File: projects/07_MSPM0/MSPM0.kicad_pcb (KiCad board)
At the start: 2 copper layers, 0 parts

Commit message: MSPM0 - Complete schematic, pass ERC checks, import footprints to PCB.
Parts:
- added C1: 10u, Capacitor_SMD:C_1206_3216Metric_Pad1.33x1.80mm_HandSolder, F.Cu at (142.1, 95.8)
- added C10: 10u, Capacitor_SMD:C_1206_3216Metric_Pad1.33x1.80mm_HandSolder, F.Cu at (160.4, 65.0)
- added C11: 470p, Capacitor_SMD:C_0603_1608Metric_Pad1.08x0.95mm_HandSolder, F.Cu at (160.4, 68.3)
- added C12: 470p, Capacitor_SMD:C_0603_1608Metric_Pad1.08x0.95mm_HandSolder, F.Cu at (141.4, 65.4)
- added C13: 470p, Capacitor_SMD:C_0603_1608Metric_Pad1.08x0.95mm_HandSolder, F.Cu at (141.4, 60.2)
- added C14: 100n, Capacitor_SMD:C_0603_1608Metric_Pad1.08x0.95mm_HandSolder, F.Cu at (201.0, 80.2)
- added C15: 100n, Capacitor_SMD:C_0603_1608Metric_Pad1.08x0.95mm_HandSolder, F.Cu at (201.0, 83.6)
- added C16: 1u, Capacitor_SMD:C_1206_3216Metric_Pad1.33x1.80mm_HandSolder, F.Cu at (179.0, 105.0)
- added C18: 10u, Capacitor_SMD:C_1206_3216Metric_Pad1.33x1.80mm_HandSolder, F.Cu at (188.5, 104.9)
- added C2: 15p, Capacitor_SMD:C_0603_1608Metric_Pad1.08x0.95mm_HandSolder, F.Cu at (134.9, 104.0)
- added C3: 470n, Capacitor_SMD:C_0603_1608Metric_Pad1.08x0.95mm_HandSolder, F.Cu at (147.7, 89.0)
- added C4: 470n, Capacitor_SMD:C_0603_1608Metric_Pad1.08x0.95mm_HandSolder, F.Cu at (137.5, 89.2)
- added C5: 470n, Capacitor_SMD:C_0603_1608Metric_Pad1.08x0.95mm_HandSolder, F.Cu at (152.5, 88.2)
- added C6: 15p, Capacitor_SMD:C_0603_1608Metric_Pad1.08x0.95mm_HandSolder, F.Cu at (142.1, 110.0)
- added C7: 470p, Capacitor_SMD:C_0603_1608Metric_Pad1.08x0.95mm_HandSolder, F.Cu at (160.4, 54.9)
- added C8: 470p, Capacitor_SMD:C_0603_1608Metric_Pad1.08x0.95mm_HandSolder, F.Cu at (160.4, 58.3)
- added C9: 10u, Capacitor_SMD:C_1206_3216Metric_Pad1.33x1.80mm_HandSolder, F.Cu at (160.4, 61.6)
- added D1: USBLC6-2SC6, Package_TO_SOT_SMD:SOT-23-6_Handsoldering, F.Cu at (122.5, 64.1)
- added D2: LED, LED_SMD:LED_1206_3216Metric_Pad1.42x1.75mm_HandSolder, F.Cu at (136.8, 70.4)
- added FID1: Fiducial, Fiducial:Fiducial_1mm_Mask2mm, F.Cu at (89.3, 92.5)
- added FID2: Fiducial, Fiducial:Fiducial_1mm_Mask2mm, F.Cu at (89.3, 96.0)
- added FID3: Fiducial, Fiducial:Fiducial_1mm_Mask2mm, F.Cu at (89.3, 99.6)
- added J1: USB_C_Receptacle_USB2.0_16P, Connector_USB:USB_C_Receptacle_G-Switch_GT-USB-7010ASV, F.Cu at (108.3, 66.6)
- added J2: Conn_ARM_SWD_TagConnect_TC2030, Connector:Tag-Connect_TC2030-IDC-FP_2x03_P1.27mm_Vertical, F.Cu at (165.8, 117.8)
- added JP1: SolderJumper_2_Bridged, Jumper:SolderJumper-2_P1.3mm_Bridged_RoundedPad1.0x1.5mm, F.Cu at (194.1, 75.2)
- added JP2: SolderJumper_2_Bridged, Jumper:SolderJumper-2_P1.3mm_Bridged_RoundedPad1.0x1.5mm, F.Cu at (191.4, 75.2)
- added JP3: SolderJumper_2_Bridged, Jumper:SolderJumper-2_P1.3mm_Bridged_RoundedPad1.0x1.5mm, F.Cu at (180.1, 99.8)
- added JP4: SolderJumper_2_Bridged, Jumper:SolderJumper-2_P1.3mm_Bridged_RoundedPad1.0x1.5mm, F.Cu at (182.7, 99.8)
- added JP5: SolderJumper_2_Bridged, Jumper:SolderJumper-2_P1.3mm_Bridged_RoundedPad1.0x1.5mm, F.Cu at (185.3, 99.8)
- added JP6: SolderJumper_2_Bridged, Jumper:SolderJumper-2_P1.3mm_Bridged_RoundedPad1.0x1.5mm, F.Cu at (184.4, 81.2)
- added JP7: SolderJumper_2_Bridged, Jumper:SolderJumper-2_P1.3mm_Bridged_RoundedPad1.0x1.5mm, F.Cu at (184.4, 83.8)
- added MH1: M3, MountingHole:MountingHole_3.2mm_M3_Pad_Via, F.Cu at (83.6, 94.7)
- added MH2: M3, MountingHole:MountingHole_3.2mm_M3_Pad_Via, F.Cu at (83.6, 102.6)
- added MH3: M3, MountingHole:MountingHole_3.2mm_M3_Pad_Via, F.Cu at (83.6, 110.6)
- added MH4: M3, MountingHole:MountingHole_3.2mm_M3_Pad_Via, F.Cu at (83.6, 118.5)
- added R1: 100k 0.1%, Resistor_SMD:R_0603_1608Metric_Pad0.98x0.95mm_HandSolder, F.Cu at (143.9, 99.0)
- added R2: 5k1, Resistor_SMD:R_0603_1608Metric_Pad0.98x0.95mm_HandSolder, F.Cu at (137.7, 93.4)
- added R3: 0R, Resistor_SMD:R_0603_1608Metric_Pad0.98x0.95mm_HandSolder, F.Cu at (152.3, 84.0)
- added R4: 0R, Resistor_SMD:R_0603_1608Metric_Pad0.98x0.95mm_HandSolder, F.Cu at (170.8, 59.4)
- added R5: 5k1, Resistor_SMD:R_0603_1608Metric_Pad0.98x0.95mm_HandSolder, F.Cu at (116.0, 49.5)
- added R6: 5k1, Resistor_SMD:R_0603_1608Metric_Pad0.98x0.95mm_HandSolder, F.Cu at (116.0, 51.2)
- added R7: 680R, Resistor_SMD:R_0603_1608Metric_Pad0.98x0.95mm_HandSolder, F.Cu at (133.2, 72.0)
- added R8: 5k1, Resistor_SMD:R_0603_1608Metric_Pad0.98x0.95mm_HandSolder, F.Cu at (147.9, 105.8)
- added R9: 5k1, Resistor_SMD:R_0603_1608Metric_Pad0.98x0.95mm_HandSolder, F.Cu at (149.7, 105.8)
- added U1: MSPM0G3507SPTR, Package_QFP:LQFP-48_7x7mm_P0.5mm, F.Cu at (150.8, 97.6)
- added U3: SPX3819M5-L-3-3, Package_TO_SOT_SMD:SOT-23-5_HandSoldering, F.Cu at (175.1, 71.0)
- added U4: CH340E, Package_SO:MSOP-10_3x3mm_P0.5mm, F.Cu at (134.4, 64.2)
- added U5: LSM6DSR, Package_LGA:LGA-14_3x2.5mm_P0.5mm_LayoutBorder3x4y, F.Cu at (192.8, 81.0)
- added U7: MMC5983MA, Package_LGA:LGA-16_3x3mm_P0.5mm, F.Cu at (183.8, 104.9)
- added Y1: 8MHz, Crystal:Crystal_SMD_3225-4Pin_3.2x2.5mm_HandSoldering, F.Cu at (141.1, 103.8)
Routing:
- net +3V3: track 0.00 -> 10.5 mm, vias 0 -> 2
- net Net-(JP3-B): track 0.00 -> 4.76 mm
- net GND: track 0.00 -> 4.30 mm, vias 0 -> 4
- net Net-(JP5-B): track 0.00 -> 4.00 mm
- net Net-(JP4-B): track 0.00 -> 3.37 mm
- net Net-(U7-CAP): track 0.00 -> 2.03 mm

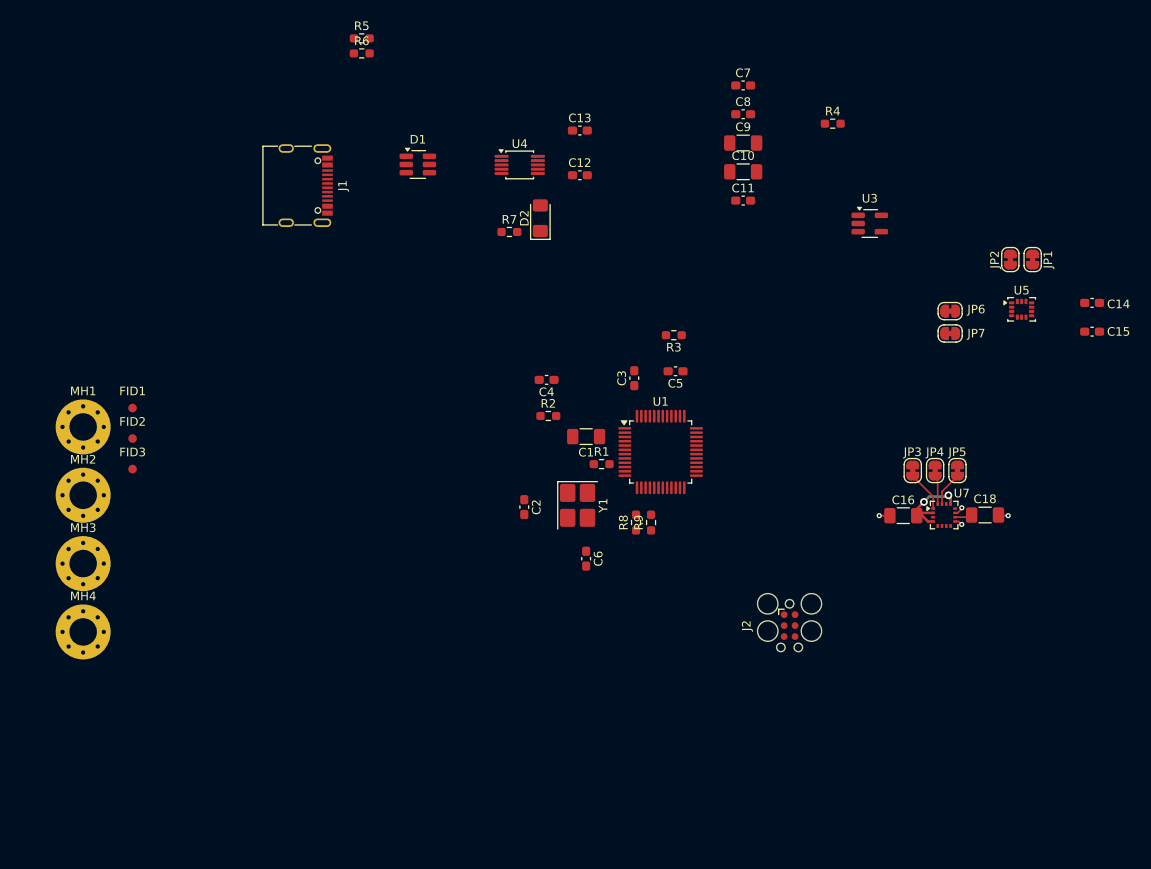
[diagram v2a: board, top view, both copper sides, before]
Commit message: MSPM0 - initialize PCB layout
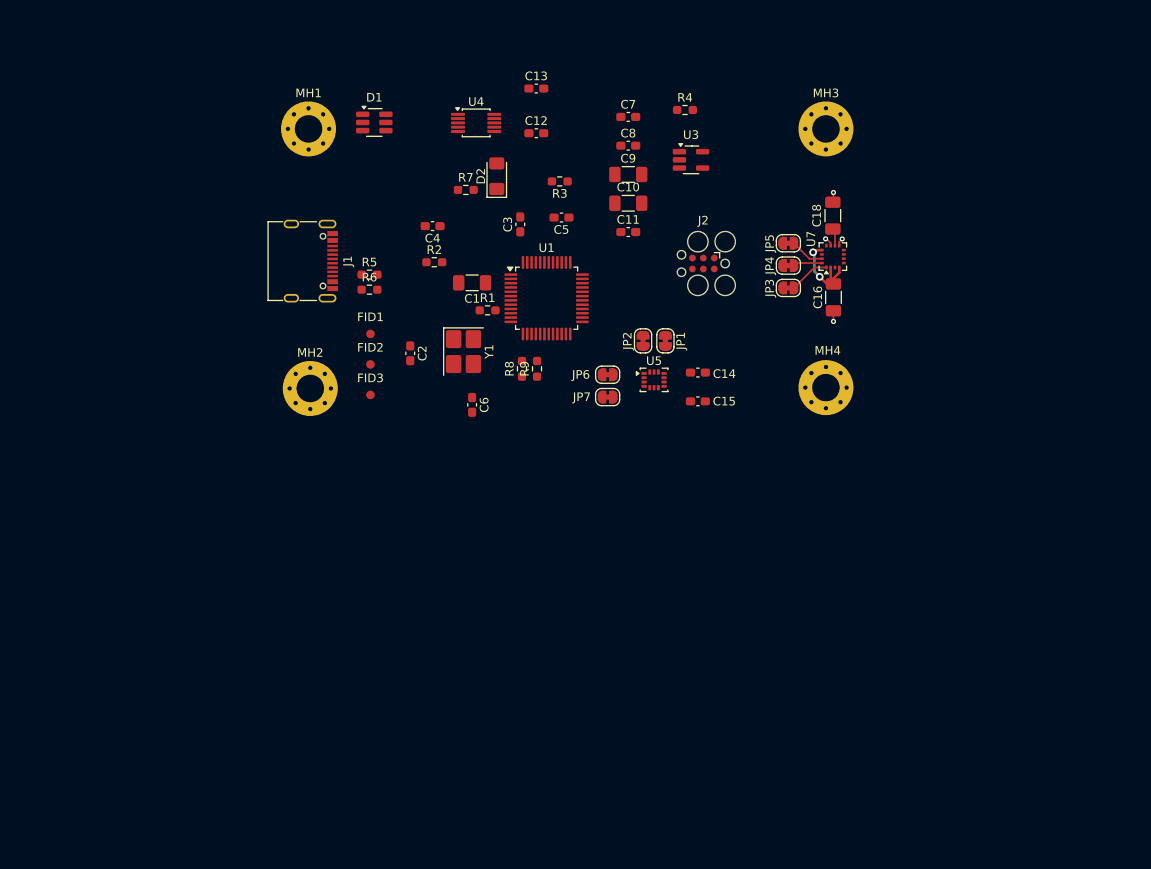
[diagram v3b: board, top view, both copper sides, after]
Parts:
- moved MH3 100.1 mm to (170.0, 60.0)
- moved MH4 91.0 mm to (170.0, 90.1)
- moved C15 46.6 mm to (155.1, 91.7)
- moved C14 46.6 mm to (155.1, 88.3)
- moved JP1 43.8 mm to (151.3, 84.7)
- moved JP2 43.8 mm to (148.7, 84.7)
- moved U5 43.5 mm to (150.0, 89.2)
- moved MH1 43.5 mm to (109.8, 60.0)
- moved J2 43.3 mm to (155.7, 75.7), turned to 180 degrees
- moved JP6 40.5 mm to (144.6, 88.6)
- moved JP7 40.5 mm to (144.6, 91.2)
- moved C18 39.1 mm to (170.8, 70.1), turned to 90 degrees
- moved JP5 33.0 mm to (165.6, 73.3), turned to 0 degrees
- moved U7 32.7 mm to (170.8, 74.9), turned to 90 degrees
- moved JP4 29.3 mm to (165.6, 75.9), turned to 0 degrees
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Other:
- rule pad_to_mask_clearance: 0 -> 0.1

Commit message: MSPM0 - Reassign pins. Add QWIIC connector for I2C. Finish placement.
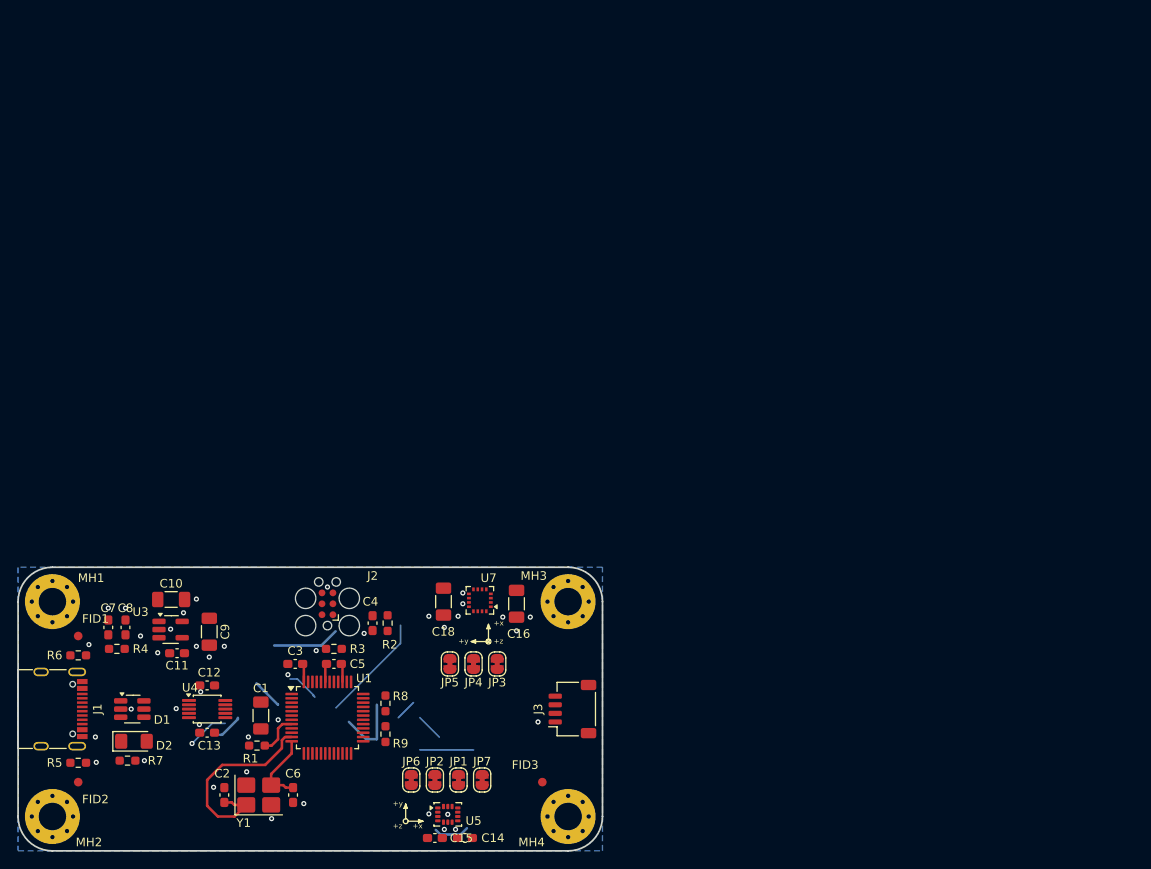
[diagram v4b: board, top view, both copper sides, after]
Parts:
- added J3: QWIIC, Connector_JST:JST_SH_SM04B-SRSS-TB_1x04-1MP_P1.00mm_Horizontal, F.Cu at (140.5, 127.5)
- moved R4 91.1 mm to (87.5, 120.5)
- moved C7 84.8 mm to (86.5, 118.0), turned to 90 degrees
- moved C13 84.2 mm to (98.0, 130.2), turned to 180 degrees
- moved U3 81.6 mm to (93.8, 118.2)
- moved C8 81.0 mm to (88.5, 118.0), turned to 90 degrees
- moved D2 78.1 mm to (89.5, 131.2), turned to 0 degrees
- moved R7 77.2 mm to (88.7, 133.5)
- moved U4 75.0 mm to (98.0, 127.5)
- moved C12 74.8 mm to (98.0, 124.8), turned to 180 degrees
- moved D1 73.8 mm to (89.3, 127.5)
- moved C9 72.2 mm to (98.2, 118.5), turned to -90 degrees
- moved C11 71.8 mm to (94.5, 121.0), turned to 180 degrees
- moved C10 70.4 mm to (93.8, 114.8)
- moved R5 66.1 mm to (83.0, 133.8)
- moved C18 63.8 mm to (125.5, 115.0), turned to -90 degrees
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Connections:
- U1 pad 14: /I2C1_SCL -> unconnected-(U1-PB2-Pad14)
- U1 pad 15: /I2C1_SDA -> unconnected-(U1-PB3-Pad15)
- U1 pad 21: /INT_MAG -> /INT1_IMU
- U1 pad 22: /INT1_IMU -> /INT2_IMU
- U1 pad 23: /INT2_IMU -> unconnected-(U1-PB9-Pad23)
- U1 pad 31: unconnected-(U1-PA16/A1_1/FCC_IN-Pad31) -> /I2C1_SDA
- U1 pad 32: unconnected-(U1-PA17/A1_2-Pad32) -> /I2C1_SCL
- U1 pad 38: unconnected-(U1-PB19/A1_6-Pad38) -> /INT_MAG
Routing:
- net /HFXIN: track 0.00 -> 23.8 mm
- net +3V3: track 10.5 -> 26.6 mm, vias 2 -> 0
- net /NRST: track 0.00 -> 12.7 mm
- net /HFXOUT: track 0.00 -> 8.76 mm
- net /INT2_IMU: track 0.00 -> 6.25 mm
- net /ROSC: track 0.00 -> 4.89 mm
- net /TNOW: track 0.00 -> 4.82 mm, vias 0 -> 1
- net Net-(JP3-B): track 4.76 -> 0.00 mm
- net GND: track 4.30 -> 0.00 mm, vias 4 -> 41
- net Net-(JP5-B): track 4.00 -> 0.00 mm
- net /SWCLK: track 0.00 -> 3.81 mm
- net Net-(JP4-B): track 3.37 -> 0.00 mm
- net /I2C1_SCL: track 0.00 -> 3.18 mm
- net /I2C1_SDA: track 0.00 -> 2.47 mm
- net /VREF-: track 0.00 -> 2.14 mm
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- added copper zone on B.Cu, net GND
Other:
- board outline added: 68 x 33 mm
